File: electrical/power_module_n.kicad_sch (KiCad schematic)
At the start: 17 parts, among them J1 Power connector for bulb driv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, J2 Need to cut return bulb wiring, J3 Ground connector from bulb wi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, Q2 BC547, Q4 IRF540N, Q5 BC557

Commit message: Updated according to recent changes
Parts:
- removed R3: 150, symbol Device:R
- added C5: ?, symbol Device:C
- added D8: 1N4002, Diode_THT:D_DO-41_SOD81_P10.16mm_Horizontal, symbol Diode:1N4002
- D1: value BZX55C 5.1V -> BZX55C 4.7V
- Q5: value BC557 -> BC557 hFE=200
- R5: value 10k -> 22k
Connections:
- net at B1.1 (-), J2.1 (Pin_1), Q4.2 (D)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: now also C5.2
- net at B1.2 (+), F1.2, J1.1 (Pin_1)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: now also C5.1, D8.2 (A)
- net at Q4.1 (G), R2.1: now also Q5.1 (C)
- net BULB DRIVE renamed BEAM_IN
- net BULB STATUS renamed BEAM_OUT
- new net POWER_12: D8.1 (K)
- no-connect marks 1 -> 0
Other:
- moved on the sheet: D1, R1, R6

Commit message: Added more readme
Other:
- title: (none) -> Power module N
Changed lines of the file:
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@@
   (paper "A4")
   (title_block
+    (title "Power module N")
     (date "2023-03-28")
   )

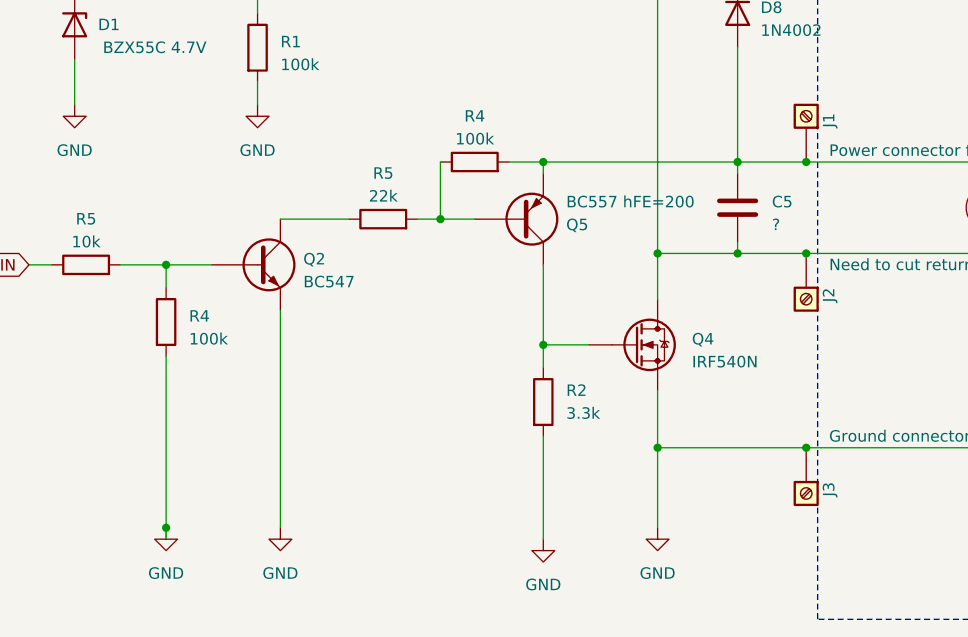
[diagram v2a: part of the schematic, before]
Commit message: Electrical diagram refactor
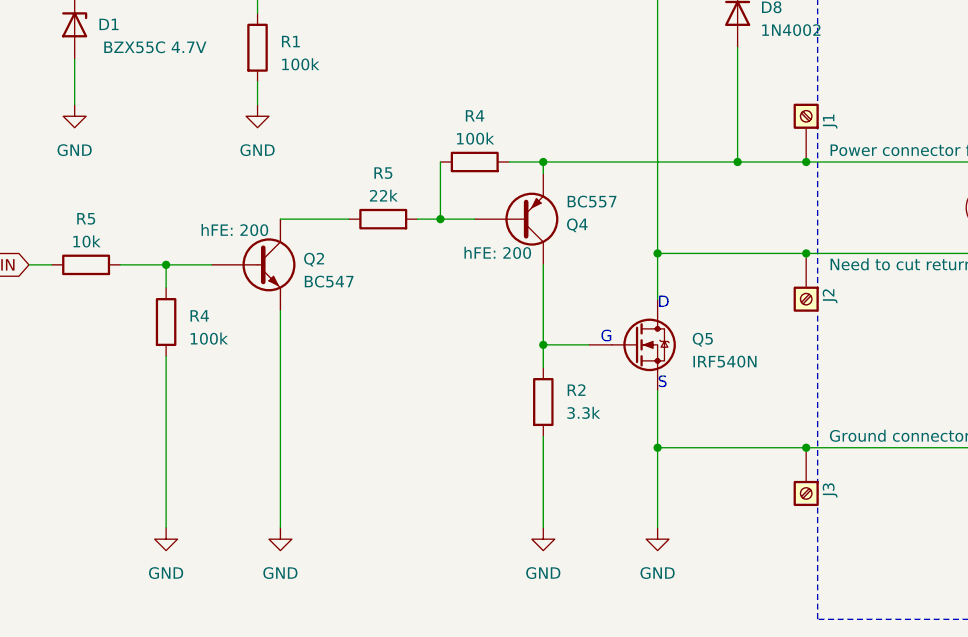
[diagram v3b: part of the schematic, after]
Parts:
- removed C5: ?, symbol Device:C
- Q2: hFE (none) -> 200
- Q4: renamed from Q5; value BC557 hFE=200 -> BC557; hFE (none) -> 200
- renumbered Q4 to Q5
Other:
- note added: "D"
- note added: "G"
- note added: "S"
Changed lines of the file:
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@@
   (junction (at 200.66 109.22) (diameter 0) (color 0 0 0 0)
   )
-  (junction (at 193.04 87.63) (diameter 0) (color 0 0 0 0)
-  )
   (junction (at 171.45 77.47) (diameter 0) (color 0 0 0 0)
   )
@@
   (junction (at 119.38 57.15) (diameter 0) (color 0 0 0 0)
   )
-  (junction (at 129.54 118.11) (diameter 0) (color 0 0 0 0)
-  )
   (junction (at 171.45 97.79) (diameter 0) (color 0 0 0 0)
   )
@@
     (stroke (width 0) (type default))
   )
-  (wire (pts (xy 171.45 107.95) (xy 171.45 119.38))
+  (wire (pts (xy 171.45 107.95) (xy 171.45 118.11))
     (stroke (width 0) (type default))
   )
@@
     (stroke (width 0) (type default))
   )
-  (wire (pts (xy 193.04 86.36) (xy 193.04 87.63))
-    (stroke (width 0) (type default))
-  )
   (wire (pts (xy 167.64 77.47) (xy 171.45 77.47))
     (stroke (width 0) (type default))
@@
     (stroke (width 0) (type default))
   )
-  (wire (pts (xy 184.15 87.63) (xy 193.04 87.63))
+  (wire (pts (xy 184.15 87.63) (xy 200.66 87.63))
     (stroke (width 0) (type default))
   )
@@
     (stroke (width 0) (type default))
   )
-  (wire (pts (xy 129.54 119.38) (xy 129.54 118.11))
+  (wire (pts (xy 129.54 99.06) (xy 129.54 118.11))
     (stroke (width 0) (type default))
   )
@@
     (stroke (width 0) (type default))
   )
-  (wire (pts (xy 193.04 78.74) (xy 193.04 77.47))
-    (stroke (width 0) (type default))
-  )
   (wire (pts (xy 171.45 97.79) (xy 176.53 97.79))
     (stroke (width 0) (type default))
@@
     (stroke (width 0) (type default))
   )
-  (wire (pts (xy 193.04 87.63) (xy 200.66 87.63))
-    (stroke (width 0) (type default))
-  )
   (wire (pts (xy 220.98 69.85) (xy 220.98 77.47))
-    (stroke (width 0) (type default))
-  )
-  (wire (pts (xy 129.54 99.06) (xy 129.54 118.11))
     (stroke (width 0) (type default))
   )
@@
   )
   (text "HEAD LO" (at 223.52 63.5 0)
+    (effects (font (size 1.27 1.27)) (justify left bottom))
+  )
+  (text "S" (at 184.15 102.87 0)
+    (effects (font (size 1.27 1.27)) (justify left bottom))
+  )
+  (text "D" (at 184.15 93.98 0)
+    (effects (font (size 1.27 1.27)) (justify left bottom))
+  )
+  (text "G" (at 177.8 97.79 0)
     (effects (font (size 1.27 1.27)) (justify left bottom))
   )
@@
         )
         (path "/01e69042-7c7e-48e9-b7c3-459316fd17f1/8dbccfbf-0961-4856-9879-280cfe95837a"
-          (reference "B2") (unit 1)
+          (reference "B1") (unit 1)
         )
       )
@@
     )
   )
-  (symbol (lib_id "Device:C") (at 193.04 82.55 0) (unit 1)
-    (in_bom yes) (on_board yes) (dnp no) (fields_autoplaced)
-    (property "Reference" "C5" (at 196.85 81.915 0)
-      (effects (font (size 1.27 1.27)) (justify left))
-    )
-    (property "Value" "?" (at 196.85 84.455 0)
-      (effects (font (size 1.27 1.27)) (justify left))
-    )
-    (property "Footprint" "" (at 194.0052 86.36 0)
-      (effects (font (size 1.27 1.27)) hide)
-    )
-    (property "Datasheet" "~" (at 193.04 82.55 0)
-      (effects (font (size 1.27 1.27)) hide)
-    )
-    (pin "1")
-    (pin "2")
-    (instances
-      (project "led_drive"
-        (path "/01e69042-7c7e-48e9-b7c3-459316fd17f1/bc381f99-814a-407f-b047-30e2660febd1"
-          (reference "C5") (unit 1)
-        )
-        (path "/01e69042-7c7e-48e9-b7c3-459316fd17f1/8dbccfbf-0961-4856-9879-280cfe95837a"
-          (reference "C8") (unit 1)
-        )
-      )
-    )
-  )
   (symbol (lib_id "Transistor_FET:IRF540N") (at 181.61 97.79 0) (unit 1)
     (in_bom yes) (on_board yes) (dnp no) (fields_autoplaced)
-    (property "Reference" "Q4" (at 187.96 97.155 0)
+    (property "Reference" "Q5" (at 187.96 97.155 0)
       (effects (font (size 1.27 1.27)) (justify left))
     )
@@
       (project "led_drive"
         (path "/01e69042-7c7e-48e9-b7c3-459316fd17f1/8dbccfbf-0961-4856-9879-280cfe95837a"
-          (reference "Q4") (unit 1)
+          (reference "Q5") (unit 1)
         )
       )
@@
         )
         (path "/01e69042-7c7e-48e9-b7c3-459316fd17f1/8dbccfbf-0961-4856-9879-280cfe95837a"
-          (reference "J11") (unit 1)
+          (reference "J1") (unit 1)
         )
       )
@@
   )
   (symbol (lib_id "Transistor_BJT:BC547") (at 139.7 88.9 0) (unit 1)
-    (in_bom yes) (on_board yes) (dnp no) (fields_autoplaced)
+    (in_bom yes) (on_board yes) (dnp no)
     (property "Reference" "Q2" (at 144.78 88.265 0)
       (effects (font (size 1.27 1.27)) (justify left))
@@
     (property "Sim.Params" "is=14340a bf=400 vaf=74.03 ikf=0.2847 ise=14340a ne=1.307 br=6.092 ikr=0 isc=0 nc=2 rb=10 rc=1 cje=22.01p vje=0.75 mje=0.377 tf=411.1p xtf=3 vtf=1.7 itf=0.6 cjc=7.306p vjc=0.75 mjc=0.3416 tr=46.91n xtb=1.5 eg=1.11 xti=3 fc=0.5" (at 139.7 88.9 0)
       (effects (font (size 1.27 1.27)) hide)
+    )
+    (property "hFE" "200" (at 137.16 85.09 0) (show_name)
+      (effects (font (size 1.27 1.27)))
     )
     (pin "1")
@@
   (symbol (lib_id "Transistor_BJT:BC557") (at 168.91 83.82 0) (mirror x) (unit 1)
     (in_bom yes) (on_board yes) (dnp no)
-    (property "Reference" "Q5" (at 173.99 84.455 0)
-      (effects (font (size 1.27 1.27)) (justify left))
-    )
-    (property "Value" "BC557 hFE=200" (at 173.99 81.915 0)
+    (property "Reference" "Q4" (at 173.99 84.455 0)
+      (effects (font (size 1.27 1.27)) (justify left))
+    )
+    (property "Value" "BC557" (at 173.99 81.915 0)
       (effects (font (size 1.27 1.27)) (justify left))
     )
@@
       (effects (font (size 1.27 1.27)) (justify left) hide)
     )
+    (property "hFE" "200" (at 166.37 87.63 0) (show_name)
+      (effects (font (size 1.27 1.27)))
+    )
     (pin "1")
     (pin "2")
@@
       (project "led_drive"
         (path "/01e69042-7c7e-48e9-b7c3-459316fd17f1/8dbccfbf-0961-4856-9879-280cfe95837a"
-          (reference "Q5") (unit 1)
+          (reference "Q4") (unit 1)
         )
       )
@@
     )
   )
-  (symbol (lib_id "power:GND") (at 171.45 119.38 0) (unit 1)
-    (in_bom yes) (on_board yes) (dnp no) (fields_autoplaced)
-    (property "Reference" "#PWR07" (at 171.45 125.73 0)
-      (effects (font (size 1.27 1.27)) hide)
-    )
-    (property "Value" "GND" (at 171.45 124.46 0)
-      (effects (font (size 1.27 1.27)))
-    )
-    (property "Footprint" "" (at 171.45 119.38 0)
-      (effects (font (size 1.27 1.27)) hide)
-    )
-    (property "Datasheet" "" (at 171.45 119.38 0)
-      (effects (font (size 1.27 1.27)) hide)
-    )
+  (symbol (lib_id "power:GND") (at 171.45 118.11 0) (unit 1)
+    (in_bom yes) (on_board yes) (dnp no) (fields_autoplaced)
+    (property "Reference" "#PWR07" (at 171.45 124.46 0)
+      (effects (font (size 1.27 1.27)) hide)
+    )
+    (property "Value" "GND" (at 171.45 123.19 0)
+      (effects (font (size 1.27 1.27)))
+    )
+    (property "Footprint" "" (at 171.45 118.11 0)
+      (effects (font (size 1.27 1.27)) hide)
+    )
+    (property "Datasheet" "" (at 171.45 118.11 0)
+      (effects (font (size 1.27 1.27)) hide)
+    )

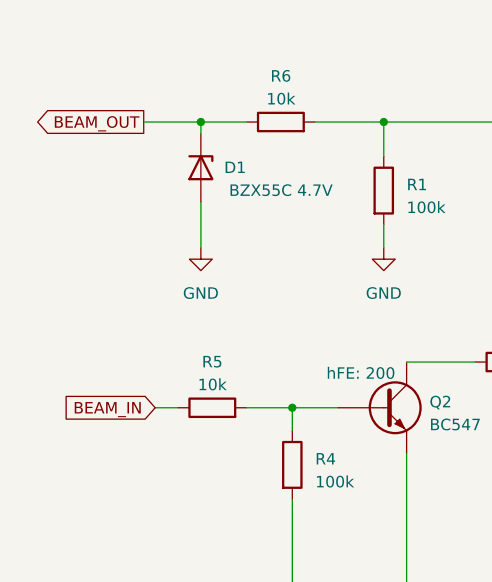
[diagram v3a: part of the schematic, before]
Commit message: What a terrible mistake - fixed BEAM IN/OUT
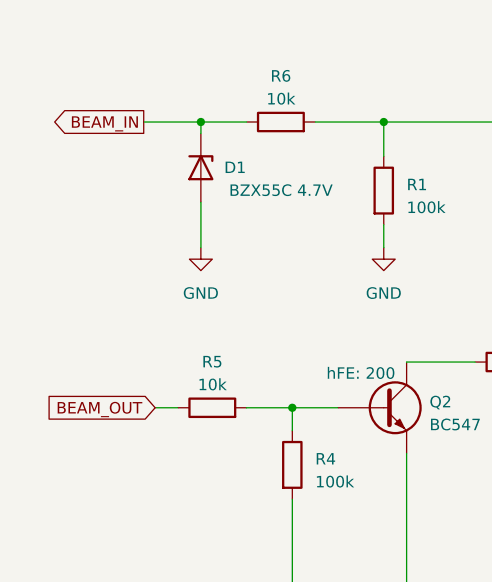
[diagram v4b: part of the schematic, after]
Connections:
- net BEAM_IN: now also D1.3 (K), R6.1; no longer R5.1
- net BEAM_OUT: now also R5.1; no longer D1.3 (K), R6.1
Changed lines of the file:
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@@
     )
   )
-  (global_label "BEAM_IN" (shape input) (at 114.3 88.9 180) (fields_autoplaced)
+  (global_label "BEAM_OUT" (shape input) (at 114.3 88.9 180) (fields_autoplaced)
     (effects (font (size 1.27 1.27)) (justify right))
-    (property "Intersheetrefs" "${INTERSHEET_REFS}" (at 103.5323 88.9 0)
+    (property "Intersheetrefs" "${INTERSHEET_REFS}" (at 101.839 88.9 0)
       (effects (font (size 1.27 1.27)) (justify right) hide)
     )
   )
-  (global_label "BEAM_OUT" (shape output) (at 113.03 57.15 180) (fields_autoplaced)
+  (global_label "BEAM_IN" (shape output) (at 113.03 57.15 180) (fields_autoplaced)
     (effects (font (size 1.27 1.27)) (justify right))
-    (property "Intersheetrefs" "${INTERSHEET_REFS}" (at 100.569 57.15 0)
+    (property "Intersheetrefs" "${INTERSHEET_REFS}" (at 102.2623 57.15 0)
       (effects (font (size 1.27 1.27)) (justify right) hide)
     )

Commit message: electrical module draft
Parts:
- removed D1: BZX55C 4.7V, Diode_THT:D_DO-35_SOD27_P7.62mm_Horizontal, symbol Diode:BZX84Cxx
- removed Q4: BC557, Package_TO_SOT_THT:TO-92_Inline, symbol Transistor_BJT:BC557
- removed R4: 100k, symbol Device:R
- added JP2: Emergency digital error ON switch, symbol Jumper:Jumper_2_Bridged
- D8: value 1N4002 -> 1N4148
- Q2: value BC547 -> BC548B
- Q5: value IRF540N -> IFRZ44N
- R1: value 100k -> 10k
- R5: value 22k -> 150
- R5: value 10k -> 2k
- R6: value 10k -> 20k
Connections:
- net GND: no longer R2.2
- net BULB: now reaches B1.1 (-), J2.1 (Pin_1), Q5.2 (D), R6.2
- net BULB: no longer R1.1
- net at B1.2 (+), D8.2 (A), F1.2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: now also R2.1, R4.1; no longer R4.2
- net at Q5.1 (G): now also R2.2, JP2.2 (B); no longer R2.1
- net at R5.2: now also JP2.1 (A); no longer R4.1
- net at Q2.2 (B), R5.2: now also R4.2
- net BEAM_IN renamed POWER_SENSE
- net POWER_SENSE: now also R1.1
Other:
- moved on the sheet: B1, D8, F1, J1, J2, J3, Q2, Q5, R1, R2, R4, R5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

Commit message: Work in progress
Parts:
- added C7: 1u, symbol Device:C
- R1: value 10k -> 100k; Tolerance (none) -> 1%
- R6: value 20k -> 200k; Tolerance (none) -> 1%
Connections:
- net GND: now also C7.2
- net BEAM_OUT renamed BULB_OUT
- net POWER_SENSE renamed BULB_SENSE
- net BULB_SENSE: now also C7.1
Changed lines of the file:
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@@
   (junction (at 109.22 66.04) (diameter 0) (color 0 0 0 0)
   )
+  (junction (at 99.06 66.04) (diameter 0) (color 0 0 0 0)
+  )
   (junction (at 171.45 119.38) (diameter 0) (color 0 0 0 0)
   )
@@
     (stroke (width 0) (type default))
   )
+  (wire (pts (xy 99.06 66.04) (xy 109.22 66.04))
+    (stroke (width 0) (type default))
+  )
   (wire (pts (xy 106.68 124.46) (xy 111.76 124.46))
     (stroke (width 0) (type default))
   )
+  (wire (pts (xy 99.06 80.01) (xy 99.06 77.47))
+    (stroke (width 0) (type default))
+  )
   (wire (pts (xy 171.45 88.9) (xy 171.45 102.87))
     (stroke (width 0) (type default))
@@
     (stroke (width 0) (type default))
   )
-  (wire (pts (xy 100.33 66.04) (xy 109.22 66.04))
+  (wire (pts (xy 92.71 66.04) (xy 99.06 66.04))
     (stroke (width 0) (type default))
   )
   (wire (pts (xy 184.15 109.22) (xy 184.15 114.3))
+    (stroke (width 0) (type default))
+  )
+  (wire (pts (xy 99.06 66.04) (xy 99.06 69.85))
     (stroke (width 0) (type default))
   )
@@
     )
   )
-  (global_label "BEAM_OUT" (shape input) (at 106.68 124.46 180) (fields_autoplaced)
+  (global_label "BULB_OUT" (shape input) (at 106.68 124.46 180) (fields_autoplaced)
     (effects (font (size 1.27 1.27)) (justify right))
     (property "Intersheetrefs" "${INTERSHEET_REFS}" (at 94.219 124.46 0)
@@
     )
   )
-  (global_label "POWER_SENSE" (shape output) (at 100.33 66.04 180) (fields_autoplaced)
+  (global_label "BULB_SENSE" (shape output) (at 92.71 66.04 180) (fields_autoplaced)
     (effects (font (size 1.27 1.27)) (justify right))
-    (property "Intersheetrefs" "${INTERSHEET_REFS}" (at 83.9382 66.04 0)
+    (property "Intersheetrefs" "${INTERSHEET_REFS}" (at 77.8905 66.04 0)
       (effects (font (size 1.27 1.27)) (justify right) hide)
     )
@@
   (symbol (lib_id "power:GND") (at 109.22 80.01 0) (unit 1)
     (in_bom yes) (on_board yes) (dnp no) (fields_autoplaced)
-    (property "Reference" "#PWR03" (at 109.22 86.36 0)
+    (property "Reference" "#PWR030" (at 109.22 86.36 0)
       (effects (font (size 1.27 1.27)) hide)
     )
@@
   (symbol (lib_id "power:GND") (at 134.62 139.7 0) (unit 1)
     (in_bom yes) (on_board yes) (dnp no) (fields_autoplaced)
-    (property "Reference" "#PWR05" (at 134.62 146.05 0)
+    (property "Reference" "#PWR032" (at 134.62 146.05 0)
       (effects (font (size 1.27 1.27)) hide)
     )
@@
         (path "/01e69042-7c7e-48e9-b7c3-459316fd17f1/8dbccfbf-0961-4856-9879-280cfe95837a"
           (reference "Q5") (unit 1)
+        )
+      )
+    )
+  )
+  (symbol (lib_id "power:GND") (at 99.06 80.01 0) (unit 1)
+    (in_bom yes) (on_board yes) (dnp no) (fields_autoplaced)
+    (property "Reference" "#PWR08" (at 99.06 86.36 0)
+      (effects (font (size 1.27 1.27)) hide)
+    )
+    (property "Value" "GND" (at 99.06 85.09 0)
+      (effects (font (size 1.27 1.27)))
+    )
+    (property "Footprint" "" (at 99.06 80.01 0)
+      (effects (font (size 1.27 1.27)) hide)
+    )
+    (property "Datasheet" "" (at 99.06 80.01 0)
+      (effects (font (size 1.27 1.27)) hide)
+    )
+    (pin "1")
+    (instances
+      (project "led_drive"
+        (path "/01e69042-7c7e-48e9-b7c3-459316fd17f1/8dbccfbf-0961-4856-9879-280cfe95837a"
+          (reference "#PWR08") (unit 1)
         )
       )
@@
   (symbol (lib_id "power:GND") (at 184.15 139.7 0) (unit 1)
     (in_bom yes) (on_board yes) (dnp no) (fields_autoplaced)
-    (property "Reference" "#PWR07" (at 184.15 146.05 0)
+    (property "Reference" "#PWR033" (at 184.15 146.05 0)
       (effects (font (size 1.27 1.27)) hide)
     )
@@
   )
   (symbol (lib_id "Device:R") (at 109.22 73.66 0) (unit 1)
-    (in_bom yes) (on_board yes) (dnp no) (fields_autoplaced)
+    (in_bom yes) (on_board yes) (dnp no)
     (property "Reference" "R1" (at 111.76 73.025 0)
       (effects (font (size 1.27 1.27)) (justify left))
     )
-    (property "Value" "10k" (at 111.76 75.565 0)
+    (property "Value" "100k" (at 111.76 75.565 0)
       (effects (font (size 1.27 1.27)) (justify left))
     )
@@
       (effects (font (size 1.27 1.27)) hide)
     )
+    (property "Tolerance" "1%" (at 113.03 77.47 0)
+      (effects (font (size 1.27 1.27)))
+    )
     (pin "1")
     (pin "2")
@@
   (symbol (lib_id "power:GND") (at 220.98 139.7 0) (unit 1)
     (in_bom yes) (on_board yes) (dnp no) (fields_autoplaced)
-    (property "Reference" "#PWR06" (at 220.98 146.05 0)
+    (property "Reference" "#PWR035" (at 220.98 146.05 0)
       (effects (font (size 1.27 1.27)) hide)
     )
@@
   )
   (symbol (lib_id "Device:R") (at 118.11 66.04 90) (unit 1)
-    (in_bom yes) (on_board yes) (dnp no) (fields_autoplaced)
+    (in_bom yes) (on_board yes) (dnp no)
     (property "Reference" "R6" (at 118.11 60.96 90)
       (effects (font (size 1.27 1.27)))
     )
-    (property "Value" "20k" (at 118.11 63.5 90)
+    (property "Value" "200k" (at 118.11 63.5 90)
       (effects (font (size 1.27 1.27)))
     )
@@
       (effects (font (size 1.27 1.27)) hide)
     )
+    (property "Tolerance" "1%" (at 118.11 68.58 90)
+      (effects (font (size 1.27 1.27)))
+    )
     (pin "1")
     (pin "2")
@@
         )
       )
+    )
+  )
+  (symbol (lib_id "Device:C") (at 99.06 73.66 0) (unit 1)
+    (in_bom yes) (on_board yes) (dnp no) (fields_autoplaced)
+    (property "Reference" "C7" (at 102.87 73.025 0)
+      (effects (font (size 1.27 1.27)) (justify left))
+    )
+    (property "Value" "1u" (at 102.87 75.565 0)
+      (effects (font (size 1.27 1.27)) (justify left))
+    )
+    (property "Footprint" "" (at 100.0252 77.47 0)
+      (effects (font (size 1.27 1.27)) hide)
+    )
+    (property "Datasheet" "~" (at 99.06 73.66 0)
+      (effects (font (size 1.27 1.27)) hide)
+    )
+    (pin "1")
+    (pin "2")
+    (instances
+      (project "led_drive"
+        (path "/01e69042-7c7e-48e9-b7c3-459316fd17f1/8dbccfbf-0961-4856-9879-280cfe95837a"
+          (reference "C7") (unit 1)
+        )
+      )

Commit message: OK, wygląda na to, że działa
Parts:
- C7: value 1u -> 100n
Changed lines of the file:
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@@
       (effects (font (size 1.27 1.27)) (justify left))
     )
-    (property "Value" "1u" (at 102.87 75.565 0)
+    (property "Value" "100n" (at 102.87 75.565 0)
       (effects (font (size 1.27 1.27)) (justify left))
     )
